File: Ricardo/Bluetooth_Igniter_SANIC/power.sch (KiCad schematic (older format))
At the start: 13 parts, among them J3 Screw_Terminal_01x02, U4 TPS63060

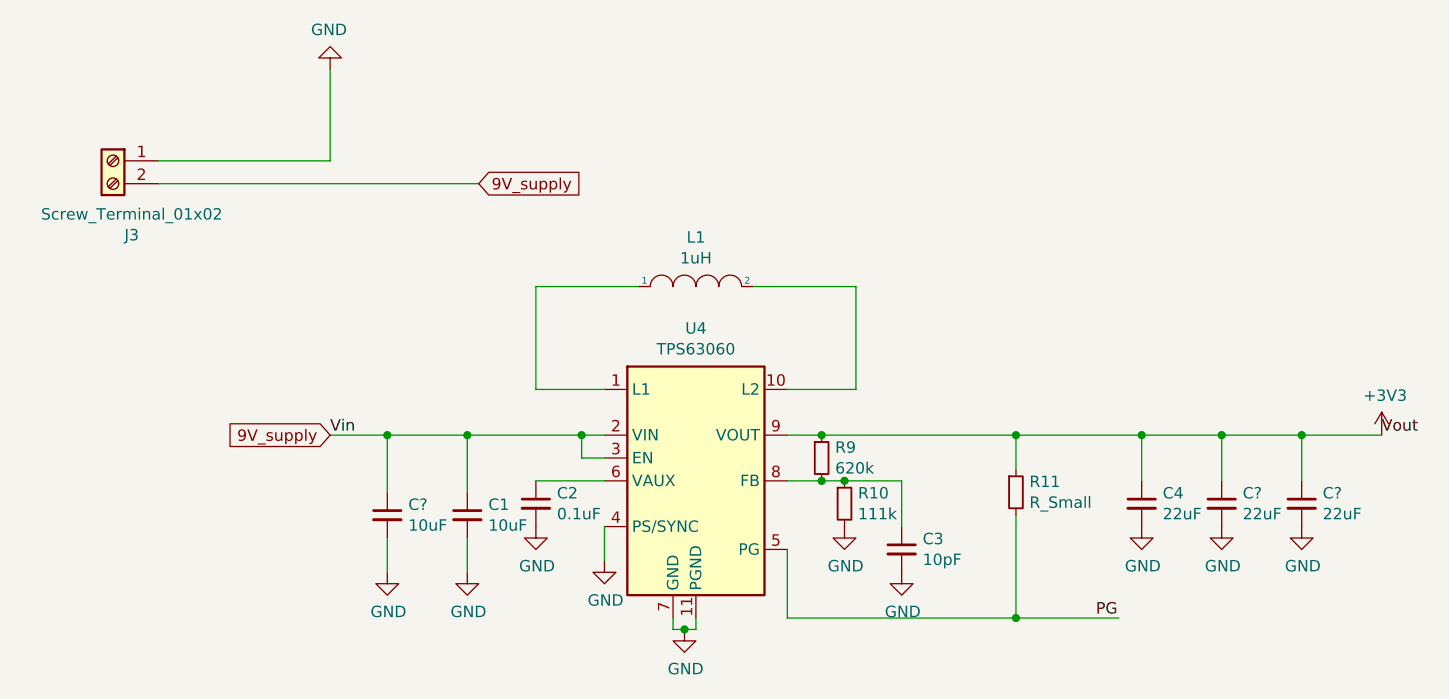
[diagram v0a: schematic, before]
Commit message: Added USB
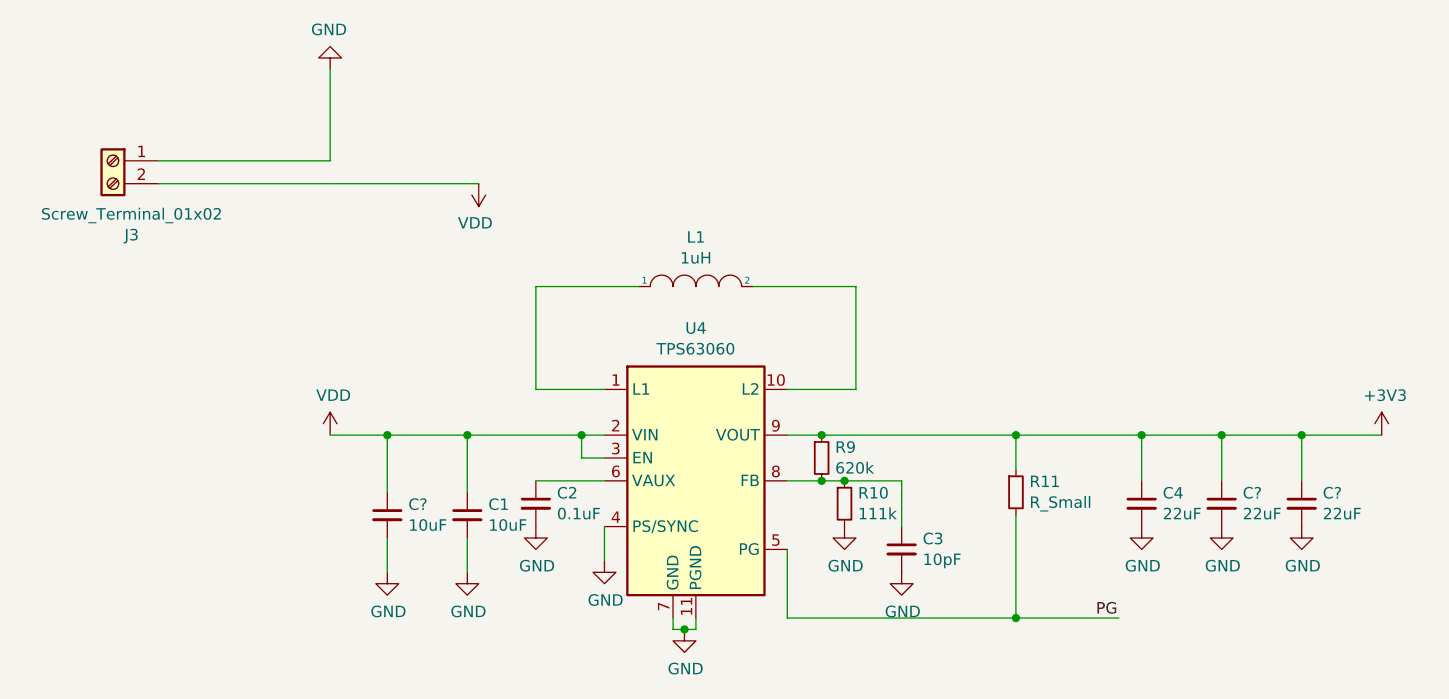
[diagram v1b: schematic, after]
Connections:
- net 9V_supply renamed VDD
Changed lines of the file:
@@
 $Descr A4 11693 8268
 encoding utf-8
-Sheet 3 3
+Sheet 3 4
 Title ""
 Date ""
@@
 	1    0    0    -1
 $EndComp
-Text Label 3600 3050 0    50   ~ 0
-Vin
-Text Label 8200 3050 0    50   ~ 0
-Vout
 $Comp
 L power:+3V3 #PWR0119
@@
 Wire Wire Line
 	2850 1950 4250 1950
-Text GLabel 4250 1950 2    50   Input ~ 0
-9V_supply
-Text GLabel 3600 3050 0    50   Input ~ 0
-9V_supply
 Wire Wire Line
 	5100 3850 5100 3900
@@
 Connection ~ 4200 3050
 Connection ~ 3850 3050
+$Comp
+L power:VDD #PWR?
+U 1 1 604AC6CE
+P 4250 1950
+F 0 "#PWR?" H 4250 1800 50  0001 C CNN
+F 1 "VDD" H 4265 2123 50  0000 C CNN
+F 2 "" H 4250 1950 50  0001 C CNN
+F 3 "" H 4250 1950 50  0001 C CNN
+	1    4250 1950
+	-1   0    0    1
+$EndComp
+$Comp
+L power:VDD #PWR?
+U 1 1 604AF69E
+P 3600 3050
+F 0 "#PWR?" H 3600 2900 50  0001 C CNN
+F 1 "VDD" H 3615 3223 50  0000 C CNN
+F 2 "" H 3600 3050 50  0001 C CNN
+F 3 "" H 3600 3050 50  0001 C CNN
+	1    3600 3050
+	1    0    0    -1
+$EndComp
 $EndSCHEMATC

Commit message: Finished schematic; starting pcb design
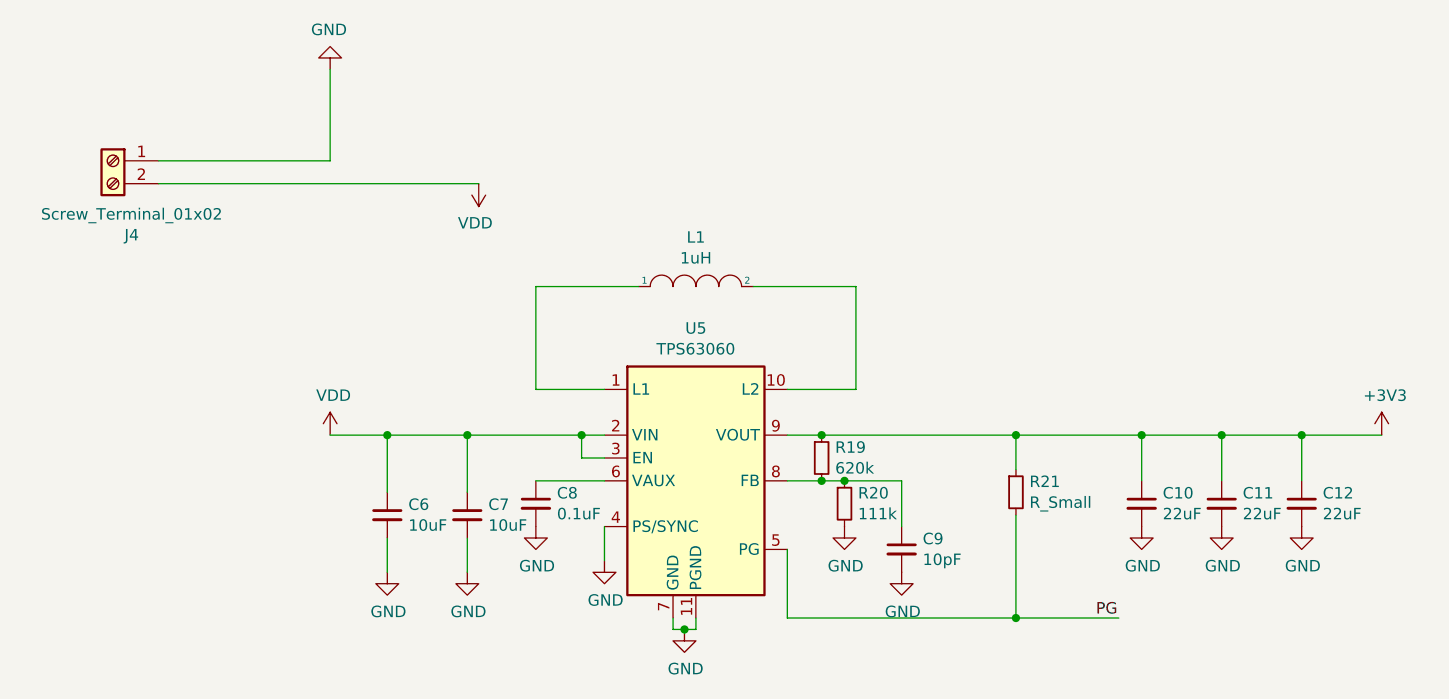
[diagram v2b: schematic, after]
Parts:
- C10: renamed from C4; footprint (none) -> Capacitor_SMD:C_0603_1608Metric
- C11, C12, C6: renamed from C?; footprint (none) -> Capacitor_SMD:C_0603_1608Metric
- C7: renamed from C1; footprint (none) -> Capacitor_SMD:C_0603_1608Metric
- C8: renamed from C2; footprint (none) -> Capacitor_SMD:C_0603_1608Metric
- C9: renamed from C3; footprint (none) -> Capacitor_SMD:C_0603_1608Metric
- J4: renamed from J3; footprint (none) -> iclrhw:PHOENIX_1757242
- L1: footprint (none) -> Inductor_SMD:L_Taiyo-Yuden_NR-30xx
- R19: renamed from R9; footprint (none) -> Resistor_SMD:R_0603_1608Metric
- R20: renamed from R10; footprint (none) -> Resistor_SMD:R_0603_1608Metric
- R21: renamed from R11; footprint (none) -> Resistor_SMD:R_0603_1608Metric
- renumbered U4 to U5
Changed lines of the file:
@@
 $Descr A4 11693 8268
 encoding utf-8
-Sheet 3 4
+Sheet 2 4
 Title ""
 Date ""
@@
 $EndDescr
 $Comp
-L Regulator_Switching:TPS63060 U4
+L Regulator_Switching:TPS63060 U5
 U 1 1 603EAA6B
 P 5200 3250
-F 0 "U4" H 5200 3917 50  0000 C CNN
+F 0 "U5" H 5200 3917 50  0000 C CNN
 F 1 "TPS63060" H 5200 3826 50  0000 C CNN
 F 2 "Package_SON:Texas_S-PWSON-N10_ThermalVias" H 5200 2600 50  0001 C CNN
@@
 F 0 "L1" H 5200 2615 50  0000 C CNN
 F 1 "1uH" H 5200 2524 50  0000 C CNN
-F 2 "" H 5200 2400 50  0001 C CNN
+F 2 "Inductor_SMD:L_Taiyo-Yuden_NR-30xx" H 5200 2400 50  0001 C CNN
 F 3 "~" H 5200 2400 50  0001 C CNN
 	1    5200 2400
@@
 	4800 3250 4500 3250
 $Comp
-L Device:R_Small R9
+L Device:R_Small R19
 U 1 1 60424E9E
 P 5750 3150
-F 0 "R9" H 5809 3196 50  0000 L CNN
+F 0 "R19" H 5809 3196 50  0000 L CNN
 F 1 "620k" H 5809 3105 50  0000 L CNN
-F 2 "" H 5750 3150 50  0001 C CNN
+F 2 "Resistor_SMD:R_0603_1608Metric" H 5750 3150 50  0001 C CNN
 F 3 "~" H 5750 3150 50  0001 C CNN
 	1    5750 3150
@@
 	5750 3250 5850 3250
 $Comp
-L Device:R_Small R11
+L Device:R_Small R21
 U 1 1 6042564C
 P 6600 3300
-F 0 "R11" H 6659 3346 50  0000 L CNN
+F 0 "R21" H 6659 3346 50  0000 L CNN
 F 1 "R_Small" H 6659 3255 50  0000 L CNN
-F 2 "" H 6600 3300 50  0001 C CNN
+F 2 "Resistor_SMD:R_0603_1608Metric" H 6600 3300 50  0001 C CNN
 F 3 "~" H 6600 3300 50  0001 C CNN
 	1    6600 3300
@@
 	6600 3200 6600 3050
 $Comp
-L Device:R_Small R10
+L Device:R_Small R20
 U 1 1 604268C6
 P 5850 3350
-F 0 "R10" H 5909 3396 50  0000 L CNN
+F 0 "R20" H 5909 3396 50  0000 L CNN
 F 1 "111k" H 5909 3305 50  0000 L CNN
-F 2 "" H 5850 3350 50  0001 C CNN
+F 2 "Resistor_SMD:R_0603_1608Metric" H 5850 3350 50  0001 C CNN
 F 3 "~" H 5850 3350 50  0001 C CNN
 	1    5850 3350
@@
 	5850 3250 6100 3250
 $Comp
-L power:GND #PWR0111
+L power:GND #PWR032
 U 1 1 6042871B
 P 5850 3450
-F 0 "#PWR0111" H 5850 3200 50  0001 C CNN
+F 0 "#PWR032" H 5850 3200 50  0001 C CNN
 F 1 "GND" H 5855 3277 50  0000 C CNN
 F 2 "" H 5850 3450 50  0001 C CNN
@@
 $EndComp
 $Comp
-L Device:C_Small C3
+L Device:C_Small C9
 U 1 1 6042A643
 P 6100 3550
-F 0 "C3" H 6192 3596 50  0000 L CNN
+F 0 "C9" H 6192 3596 50  0000 L CNN
 F 1 "10pF" H 6192 3505 50  0000 L CNN
-F 2 "" H 6100 3550 50  0001 C CNN
+F 2 "Capacitor_SMD:C_0603_1608Metric" H 6100 3550 50  0001 C CNN
 F 3 "~" H 6100 3550 50  0001 C CNN
 	1    6100 3550
@@
 	5750 3050 6600 3050
 $Comp
-L power:GND #PWR0112
+L power:GND #PWR033
 U 1 1 6042C935
 P 6100 3650
-F 0 "#PWR0112" H 6100 3400 50  0001 C CNN
+F 0 "#PWR033" H 6100 3400 50  0001 C CNN
 F 1 "GND" H 6105 3477 50  0000 C CNN
 F 2 "" H 6100 3650 50  0001 C CNN
@@
 Connection ~ 7150 3050
 $Comp
-L Device:C_Small C4
+L Device:C_Small C10
 U 1 1 6042D8E9
 P 7150 3350
-F 0 "C4" H 7242 3396 50  0000 L CNN
+F 0 "C10" H 7242 3396 50  0000 L CNN
 F 1 "22uF" H 7242 3305 50  0000 L CNN
-F 2 "" H 7150 3350 50  0001 C CNN
+F 2 "Capacitor_SMD:C_0603_1608Metric" H 7150 3350 50  0001 C CNN
 F 3 "~" H 7150 3350 50  0001 C CNN
 	1    7150 3350
@@
 $EndComp
 $Comp
-L power:GND #PWR0113
+L power:GND #PWR034
 U 1 1 6042E1A4
 P 7150 3450
-F 0 "#PWR0113" H 7150 3200 50  0001 C CNN
+F 0 "#PWR034" H 7150 3200 50  0001 C CNN
 F 1 "GND" H 7155 3277 50  0000 C CNN
 F 2 "" H 7150 3450 50  0001 C CNN
@@
 	4800 3450 4800 3600
 $Comp
-L power:GND #PWR0116
+L power:GND #PWR030
 U 1 1 604347BE
 P 4800 3600
-F 0 "#PWR0116" H 4800 3350 50  0001 C CNN
+F 0 "#PWR030" H 4800 3350 50  0001 C CNN
 F 1 "GND" H 4805 3427 50  0000 C CNN
 F 2 "" H 4800 3600 50  0001 C CNN
@@
 $EndComp
 $Comp
-L Device:C_Small C2
+L Device:C_Small C8
 U 1 1 60435134
 P 4500 3350
-F 0 "C2" H 4592 3396 50  0000 L CNN
+F 0 "C8" H 4592 3396 50  0000 L CNN
 F 1 "0.1uF" H 4592 3305 50  0000 L CNN
-F 2 "" H 4500 3350 50  0001 C CNN
+F 2 "Capacitor_SMD:C_0603_1608Metric" H 4500 3350 50  0001 C CNN
 F 3 "~" H 4500 3350 50  0001 C CNN
 	1    4500 3350
@@
 $EndComp
 $Comp
-L power:GND #PWR0117
+L power:GND #PWR029
 U 1 1 60435A81
 P 4500 3450
-F 0 "#PWR0117" H 4500 3200 50  0001 C CNN
+F 0 "#PWR029" H 4500 3200 50  0001 C CNN
 F 1 "GND" H 4505 3277 50  0000 C CNN
 F 2 "" H 4500 3450 50  0001 C CNN
@@
 	4200 3050 4200 3300
 $Comp
-L Device:C_Small C1
+L Device:C_Small C7
 U 1 1 60436971
 P 4200 3400
-F 0 "C1" H 4292 3446 50  0000 L CNN
+F 0 "C7" H 4292 3446 50  0000 L CNN
 F 1 "10uF" H 4292 3355 50  0000 L CNN
-F 2 "" H 4200 3400 50  0001 C CNN
+F 2 "Capacitor_SMD:C_0603_1608Metric" H 4200 3400 50  0001 C CNN
 F 3 "~" H 4200 3400 50  0001 C CNN
 	1    4200 3400
@@
 	4200 3500 4200 3650
 $Comp
-L power:GND #PWR0118
+L power:GND #PWR027
 U 1 1 604370BE
 P 4200 3650
-F 0 "#PWR0118" H 4200 3400 50  0001 C CNN
+F 0 "#PWR027" H 4200 3400 50  0001 C CNN
 F 1 "GND" H 4205 3477 50  0000 C CNN
 F 2 "" H 4200 3650 50  0001 C CNN
@@
 $EndComp
 $Comp
-L power:+3V3 #PWR0119
+L power:+3V3 #PWR037
 U 1 1 60439764
 P 8200 3050
-F 0 "#PWR0119" H 8200 2900 50  0001 C CNN
+F 0 "#PWR037" H 8200 2900 50  0001 C CNN
 F 1 "+3V3" H 8215 3223 50  0000 C CNN
 F 2 "" H 8200 3050 50  0001 C CNN
@@
 $EndComp
 $Comp
-L Connector:Screw_Terminal_01x02 J3
+L Connector:Screw_Terminal_01x02 J4
 U 1 1 60437B13
 P 2650 1850
-F 0 "J3" H 2568 1525 50  0000 C CNN
+F 0 "J4" H 2568 1525 50  0000 C CNN
 F 1 "Screw_Terminal_01x02" H 2568 1616 50  0000 C CNN
-F 2 "" H 2650 1850 50  0001 C CNN
+F 2 "iclrhw:PHOENIX_1757242" H 2650 1850 50  0001 C CNN
 F 3 "~" H 2650 1850 50  0001 C CNN
 	1    2650 1850
@@
 	3600 1850 3600 1450
 $Comp
-L power:GND #PWR0120
+L power:GND #PWR024
 U 1 1 6043B88B
 P 3600 1450
-F 0 "#PWR0120" H 3600 1200 50  0001 C CNN
+F 0 "#PWR024" H 3600 1200 50  0001 C CNN
 F 1 "GND" H 3605 1277 50  0000 C CNN
 F 2 "" H 3600 1450 50  0001 C CNN
@@
 	5200 3900 5200 3850
 $Comp
-L power:GND #PWR?
+L power:GND #PWR031
 U 1 1 60452734
 P 5150 3900
-F 0 "#PWR?" H 5150 3650 50  0001 C CNN
+F 0 "#PWR031" H 5150 3650 50  0001 C CNN
 F 1 "GND" H 5155 3727 50  0000 C CNN
 F 2 "" H 5150 3900 50  0001 C CNN
@@
 	7150 3050 7500 3050
 $Comp
-L Device:C_Small C?
+L Device:C_Small C11
 U 1 1 60497866
 P 7500 3350
-F 0 "C?" H 7592 3396 50  0000 L CNN
+F 0 "C11" H 7592 3396 50  0000 L CNN
 F 1 "22uF" H 7592 3305 50  0000 L CNN
-F 2 "" H 7500 3350 50  0001 C CNN
+F 2 "Capacitor_SMD:C_0603_1608Metric" H 7500 3350 50  0001 C CNN
 F 3 "~" H 7500 3350 50  0001 C CNN
 	1    7500 3350
@@
 $EndComp
 $Comp
-L power:GND #PWR?
+L power:GND #PWR035
 U 1 1 6049786C
 P 7500 3450
-F 0 "#PWR?" H 7500 3200 50  0001 C CNN
+F 0 "#PWR035" H 7500 3200 50  0001 C CNN
 F 1 "GND" H 7505 3277 50  0000 C CNN
 F 2 "" H 7500 3450 50  0001 C CNN
@@
 $EndComp
 $Comp
-L Device:C_Small C?
+L Device:C_Small C12
 U 1 1 60498C8D
 P 7850 3350
-F 0 "C?" H 7942 3396 50  0000 L CNN
+F 0 "C12" H 7942 3396 50  0000 L CNN
 F 1 "22uF" H 7942 3305 50  0000 L CNN
-F 2 "" H 7850 3350 50  0001 C CNN
+F 2 "Capacitor_SMD:C_0603_1608Metric" H 7850 3350 50  0001 C CNN
 F 3 "~" H 7850 3350 50  0001 C CNN
 	1    7850 3350
@@
 $EndComp
 $Comp
-L power:GND #PWR?
+L power:GND #PWR036
 U 1 1 60498C93
 P 7850 3450
-F 0 "#PWR?" H 7850 3200 50  0001 C CNN
+F 0 "#PWR036" H 7850 3200 50  0001 C CNN
 F 1 "GND" H 7855 3277 50  0000 C CNN
 F 2 "" H 7850 3450 50  0001 C CNN
@@
 	3850 3050 3850 3300
 $Comp
-L Device:C_Small C?
+L Device:C_Small C6
 U 1 1 6049C9AB
 P 3850 3400
-F 0 "C?" H 3942 3446 50  0000 L CNN
+F 0 "C6" H 3942 3446 50  0000 L CNN
 F 1 "10uF" H 3942 3355 50  0000 L CNN
-F 2 "" H 3850 3400 50  0001 C CNN
+F 2 "Capacitor_SMD:C_0603_1608Metric" H 3850 3400 50  0001 C CNN
 F 3 "~" H 3850 3400 50  0001 C CNN
 	1    3850 3400
@@
 	3850 3500 3850 3650
 $Comp
-L power:GND #PWR?
+L power:GND #PWR026
 U 1 1 6049C9B2
 P 3850 3650
-F 0 "#PWR?" H 3850 3400 50  0001 C CNN
+F 0 "#PWR026" H 3850 3400 50  0001 C CNN
 F 1 "GND" H 3855 3477 50  0000 C CNN
 F 2 "" H 3850 3650 50  0001 C CNN
@@
 Connection ~ 3850 3050
 $Comp
-L power:VDD #PWR?
+L power:VDD #PWR028
 U 1 1 604AC6CE
 P 4250 1950
-F 0 "#PWR?" H 4250 1800 50  0001 C CNN
+F 0 "#PWR028" H 4250 1800 50  0001 C CNN
 F 1 "VDD" H 4265 2123 50  0000 C CNN
 F 2 "" H 4250 1950 50  0001 C CNN
@@
 $EndComp
 $Comp
-L power:VDD #PWR?
+L power:VDD #PWR025
 U 1 1 604AF69E
 P 3600 3050
-F 0 "#PWR?" H 3600 2900 50  0001 C CNN
+F 0 "#PWR025" H 3600 2900 50  0001 C CNN
 F 1 "VDD" H 3615 3223 50  0000 C CNN
 F 2 "" H 3600 3050 50  0001 C CNN
